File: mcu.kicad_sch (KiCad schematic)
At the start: 16 parts, among them J2 USB_C_Receptacle_USB2.0, J3 SH-6P, SW1 SW_Push, SW2 SW_Push, U3 TJA1051TK-3, U4 STM32G0B1KBU6

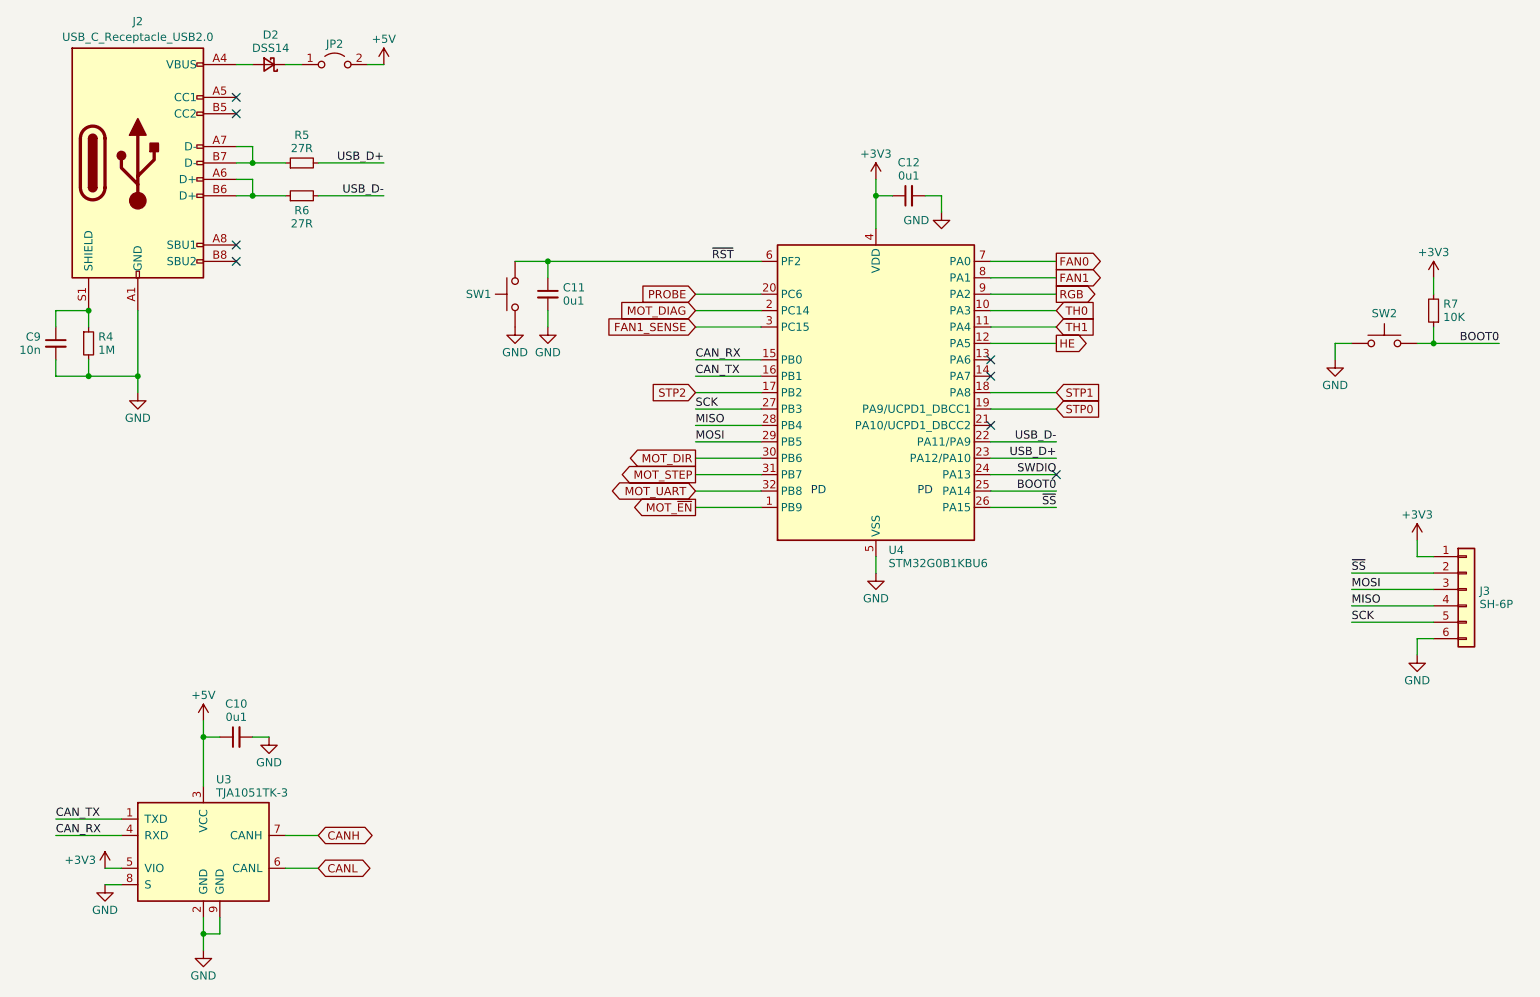
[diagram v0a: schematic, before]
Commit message: Added solder jumpers for CAN/USB interface selection
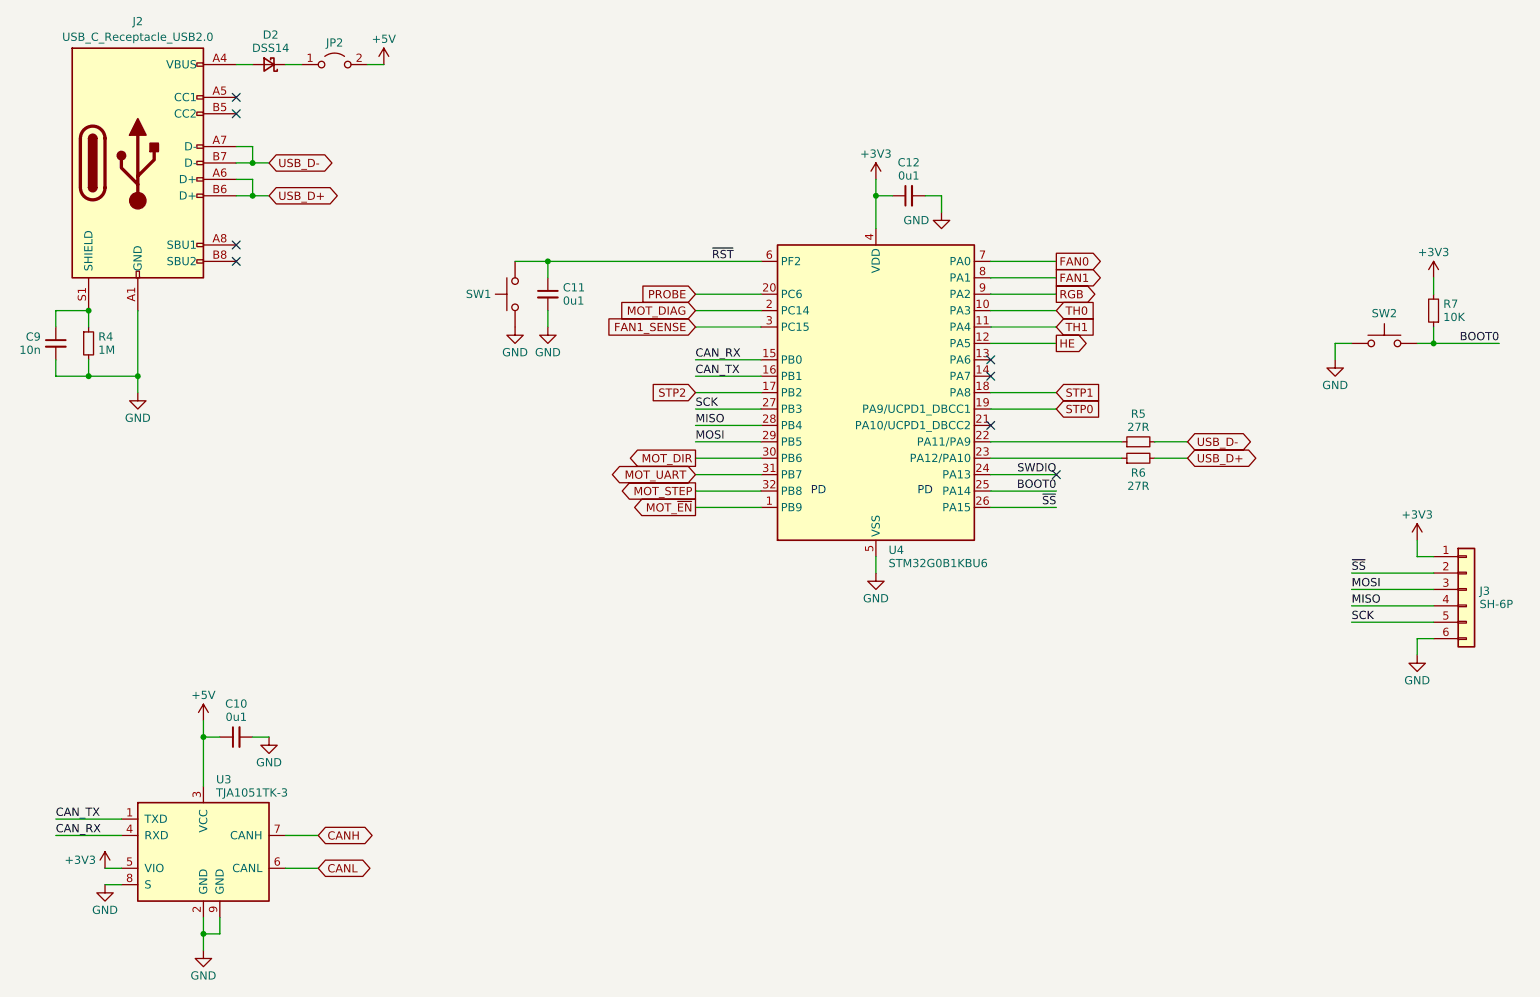
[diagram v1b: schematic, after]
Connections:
- net MOT_STEP: now also U4.32 (PB8); no longer U4.31 (PB7)
- net MOT_UART: now also U4.31 (PB7); no longer U4.32 (PB8)
- net USB_D+: now also J2.A6 (D+), J2.B6 (D+), R6.2; no longer R5.2, U4.23 (PA12/PA10)
- net USB_D-: now also J2.A7 (D-), J2.B7 (D-), R5.2; no longer R6.2, U4.22 (PA11/PA9)
- new net: R5.1, U4.22 (PA11/PA9)
- new net: R6.1, U4.23 (PA12/PA10)
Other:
- moved on the sheet: R5, R6
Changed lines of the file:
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@@
 	(paper "A4")
+	(junction
+		(at 50.8 137.16)
+		(diameter 0)
+		(color 0 0 0 0)
+	)
+	(junction
+		(at 241.3 76.2)
+		(diameter 0)
+		(color 0 0 0 0)
+	)
+	(junction
+		(at 40.64 81.28)
+		(diameter 0)
+		(color 0 0 0 0)
+	)
+	(junction
+		(at 50.8 167.64)
+		(diameter 0)
+		(color 0 0 0 0)
+	)
+	(junction
+		(at 154.94 53.34)
+		(diameter 0)
+		(color 0 0 0 0)
+	)
 	(junction
 		(at 58.42 53.34)
@@
 	)
 	(junction
-		(at 50.8 137.16)
+		(at 33.02 71.12)
 		(diameter 0)
 		(color 0 0 0 0)
 	)
 	(junction
-		(at 241.3 76.2)
-		(diameter 0)
-		(color 0 0 0 0)
-	)
-	(junction
-		(at 40.64 81.28)
-		(diameter 0)
-		(color 0 0 0 0)
-	)
-	(junction
-		(at 50.8 167.64)
-		(diameter 0)
-		(color 0 0 0 0)
-	)
-	(junction
-		(at 154.94 53.34)
-		(diameter 0)
-		(color 0 0 0 0)
-	)
-	(junction
-		(at 33.02 71.12)
+		(at 58.42 48.26)
 		(diameter 0)
 		(color 0 0 0 0)
@@
 		(color 0 0 0 0)
 	)
-	(junction
-		(at 58.42 48.26)
-		(diameter 0)
-		(color 0 0 0 0)
-	)
 	(no_connect
 		(at 172.72 88.9)
@@
 	(wire
 		(pts
+			(xy 58.42 48.26) (xy 60.96 48.26)
+		)
+		(stroke
+			(width 0)
+			(type default)
+		)
+	)
+	(wire
+		(pts
 			(xy 27.94 81.28) (xy 27.94 78.74)
 		)
@@
 	(wire
 		(pts
-			(xy 172.72 93.98) (xy 182.88 93.98)
+			(xy 172.72 93.98) (xy 193.04 93.98)
 		)
 		(stroke
@@
 	(wire
 		(pts
+			(xy 58.42 53.34) (xy 60.96 53.34)
+		)
+		(stroke
+			(width 0)
+			(type default)
+		)
+	)
+	(wire
+		(pts
 			(xy 137.16 86.36) (xy 127 86.36)
 		)
@@
 	(wire
 		(pts
-			(xy 172.72 91.44) (xy 182.88 91.44)
+			(xy 172.72 91.44) (xy 193.04 91.44)
 		)
 		(stroke
@@
 	(wire
 		(pts
-			(xy 68.58 53.34) (xy 78.74 53.34)
+			(xy 198.12 93.98) (xy 203.2 93.98)
 		)
 		(stroke
@@
 	(wire
 		(pts
-			(xy 58.42 48.26) (xy 63.5 48.26)
-		)
-		(stroke
-			(width 0)
-			(type default)
-		)
-	)
-	(wire
-		(pts
 			(xy 53.34 165.1) (xy 53.34 167.64)
 		)
@@
 	(wire
 		(pts
-			(xy 68.58 48.26) (xy 78.74 48.26)
+			(xy 198.12 91.44) (xy 203.2 91.44)
 		)
 		(stroke
@@
 		(pts
 			(xy 172.72 73.66) (xy 182.88 73.66)
-		)
-		(stroke
-			(width 0)
-			(type default)
-		)
-	)
-	(wire
-		(pts
-			(xy 58.42 53.34) (xy 63.5 53.34)
 		)
 		(stroke
@@
 		)
 	)
-	(label "USB_D+"
-		(at 182.88 93.98 180)
-		(fields_autoplaced yes)
-		(effects
-			(font
-				(size 1.27 1.27)
-			)
-			(justify right bottom)
-		)
-	)
 	(label "CAN_RX"
 		(at 127 78.74 0)
@@
 		)
 	)
-	(label "USB_D-"
-		(at 78.74 53.34 180)
-		(fields_autoplaced yes)
-		(effects
-			(font
-				(size 1.27 1.27)
-			)
-			(justify right bottom)
-		)
-	)
 	(label "CAN_TX"
 		(at 27.94 149.86 0)
@@
 		)
 	)
-	(label "USB_D-"
-		(at 182.88 91.44 180)
-		(fields_autoplaced yes)
-		(effects
-			(font
-				(size 1.27 1.27)
-			)
-			(justify right bottom)
-		)
-	)
 	(label "CAN_TX"
 		(at 127 81.28 0)
@@
 		)
 	)
-	(label "USB_D+"
-		(at 78.74 48.26 180)
-		(fields_autoplaced yes)
-		(effects
-			(font
-				(size 1.27 1.27)
-			)
-			(justify right bottom)
-		)
-	)
 	(label "BOOT0"
 		(at 182.88 99.06 180)
@@
 			)
 			(justify left bottom)
+		)
+	)
+	(global_label "USB_D+"
+		(shape bidirectional)
+		(at 203.2 93.98 0)
+		(fields_autoplaced yes)
+		(effects
+			(font
+				(size 1.27 1.27)
+			)
+			(justify left)
+		)
+		(property "Intersheetrefs" "${INTERSHEET_REFS}"
+			(at 214.9165 93.98 0)
+			(effects
+				(font
+					(size 1.27 1.27)
+				)
+				(justify left)
+				(hide yes)
+			)
 		)
 	)
@@
 		)
 	)
+	(global_label "USB_D-"
+		(shape bidirectional)
+		(at 60.96 48.26 0)
+		(fields_autoplaced yes)
+		(effects
+			(font
+				(size 1.27 1.27)
+			)
+			(justify left)
+		)
+		(property "Intersheetrefs" "${INTERSHEET_REFS}"
+			(at 72.6765 48.26 0)
+			(effects
+				(font
+					(size 1.27 1.27)
+				)
+				(justify left)
+				(hide yes)
+			)
+		)
+	)
 	(global_label "MOT_UART"
 		(shape bidirectional)
-		(at 127 99.06 180)
+		(at 127 96.52 180)
 		(fields_autoplaced yes)
 		(effects
@@
 		)
 		(property "Intersheetrefs" "${INTERSHEET_REFS}"
-			(at 113.6091 99.06 0)
+			(at 113.6091 96.52 0)
 			(effects
 				(font
@@
 	(global_label "MOT_STEP"
 		(shape output)
-		(at 127 96.52 180)
+		(at 127 99.06 180)
 		(fields_autoplaced yes)
 		(effects
@@
 		)
 		(property "Intersheetrefs" "${INTERSHEET_REFS}"
-			(at 114.781 96.52 0)
+			(at 114.781 99.06 0)
 			(effects
 				(font
@@
 				)
 				(justify right)
+				(hide yes)
+			)
+		)
+	)
+	(global_label "USB_D-"
+		(shape bidirectional)
+		(at 203.2 91.44 0)
+		(fields_autoplaced yes)
+		(effects
+			(font
+				(size 1.27 1.27)
+			)
+			(justify left)
+		)
+		(property "Intersheetrefs" "${INTERSHEET_REFS}"
+			(at 214.9165 91.44 0)
+			(effects
+				(font
+					(size 1.27 1.27)
+				)
+				(justify left)
+				(hide yes)
+			)
+		)
+	)
+	(global_label "USB_D+"
+		(shape bidirectional)
+		(at 60.96 53.34 0)
+		(fields_autoplaced yes)
+		(effects
+			(font
+				(size 1.27 1.27)
+			)
+			(justify left)
+		)
+		(property "Intersheetrefs" "${INTERSHEET_REFS}"
+			(at 72.6765 53.34 0)
+			(effects
+				(font
+					(size 1.27 1.27)
+				)
+				(justify left)
 				(hide yes)
 			)
@@
 		(fields_autoplaced yes)
 		(property "Reference" "JP2"
-			(at 71.12 29.837 0)
+			(at 71.12 29.6489 0)
 			(effects
 				(font
@@
 			)
 		)
-		(property "Description" ""
+		(property "Description" "Jumper, 2-pole, open"
 			(at 71.12 33.02 0)
 			(effects
@@
 	(symbol
 		(lib_id "Device:R_Small")
-		(at 66.04 48.26 90)
+		(at 195.58 91.44 90)
 		(unit 1)
 		(exclude_from_sim no)
@@
 		(fields_autoplaced yes)
 		(property "Reference" "R5"
-			(at 66.04 43.9434 90)
+			(at 195.58 87.1234 90)
 			(effects
 				(font
@@
 		)
 		(property "Value" "27R"
-			(at 66.04 45.9914 90)
+			(at 195.58 89.1714 90)
 			(effects
 				(font
@@
 		)
 		(property "Footprint" "Resistor_SMD:R_0402_1005Metric"
-			(at 66.04 48.26 0)
+			(at 195.58 91.44 0)
 			(effects
 				(font
@@
 		)
 		(property "Datasheet" "~"
-			(at 66.04 48.26 0)
+			(at 195.58 91.44 0)
 			(effects
 				(font
@@
 		)
 		(property "Description" ""
-			(at 66.04 48.26 0)
+			(at 195.58 91.44 0)
 			(effects
 				(font
@@
 		)
 		(property "MPN" ""
-			(at 66.04 48.26 0)
+			(at 195.58 91.44 0)
 			(effects
 				(font
@@
 		)
 		(property "LCSC" "C25100"
-			(at 66.04 48.26 0)
+			(at 195.58 91.44 0)
 			(effects
 				(font
@@
 	(symbol
 		(lib_id "Device:R_Small")
-		(at 66.04 53.34 90)
+		(at 195.58 93.98 90)
 		(unit 1)
 		(exclude_from_sim no)
@@
 		(fields_autoplaced yes)
 		(property "Reference" "R6"
-			(at 66.04 55.6086 90)
+			(at 195.58 96.2486 90)
 			(effects
 				(font
@@
 		)
 		(property "Value" "27R"
-			(at 66.04 57.6566 90)
+			(at 195.58 98.2966 90)
 			(effects
 				(font
@@
 		)
 		(property "Footprint" "Resistor_SMD:R_0402_1005Metric"
-			(at 66.04 53.34 0)
+			(at 195.58 93.98 0)
 			(effects
 				(font
@@
 		)
 		(property "Datasheet" "~"
-			(at 66.04 53.34 0)
+			(at 195.58 93.98 0)
 			(effects
 				(font
@@
 		)
 		(property "Description" ""
-			(at 66.04 53.34 0)
+			(at 195.58 93.98 0)
 			(effects
 				(font
@@
 		)
 		(property "MPN" ""
-			(at 66.04 53.34 0)
+			(at 195.58 93.98 0)
 			(effects
 				(font
@@
 		)
 		(property "LCSC" "C25100"
-			(at 66.04 53.34 0)
-			(effects
-				(font
+			(at 195.58 93.98 0)
+			(effects
+				(font

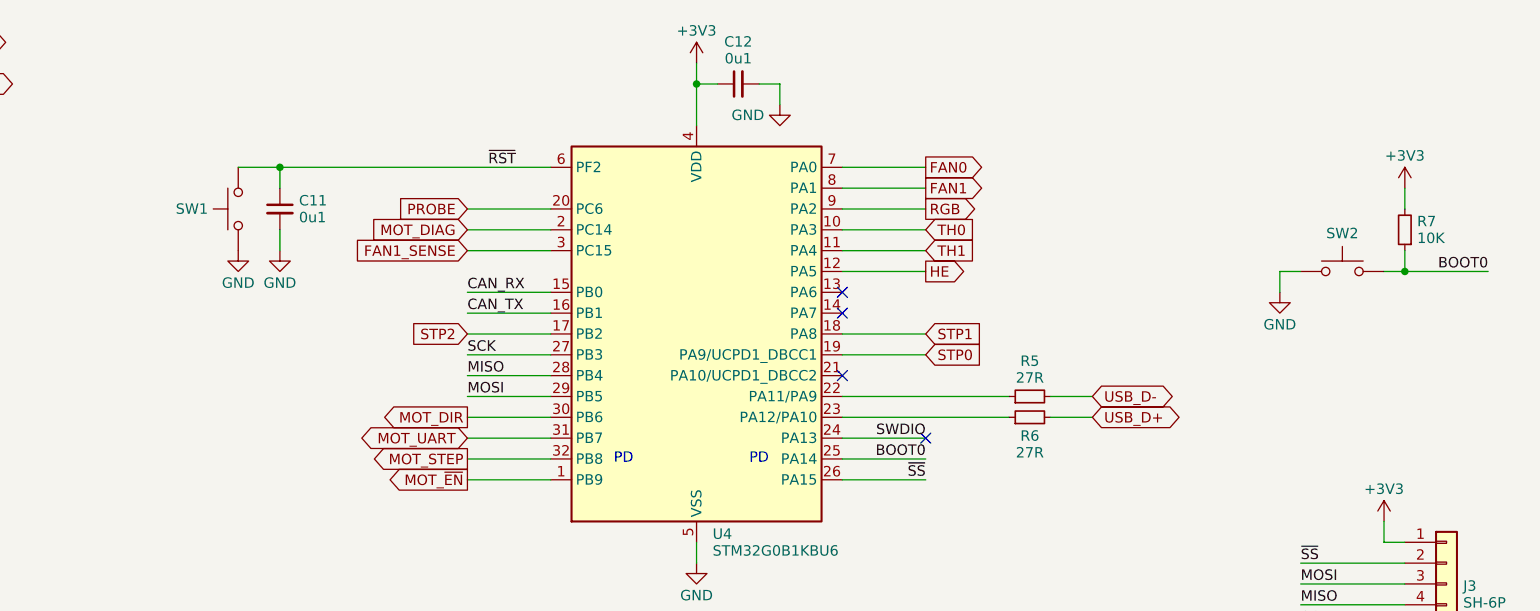
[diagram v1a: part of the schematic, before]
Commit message: Layout tweaks/pinout optimization
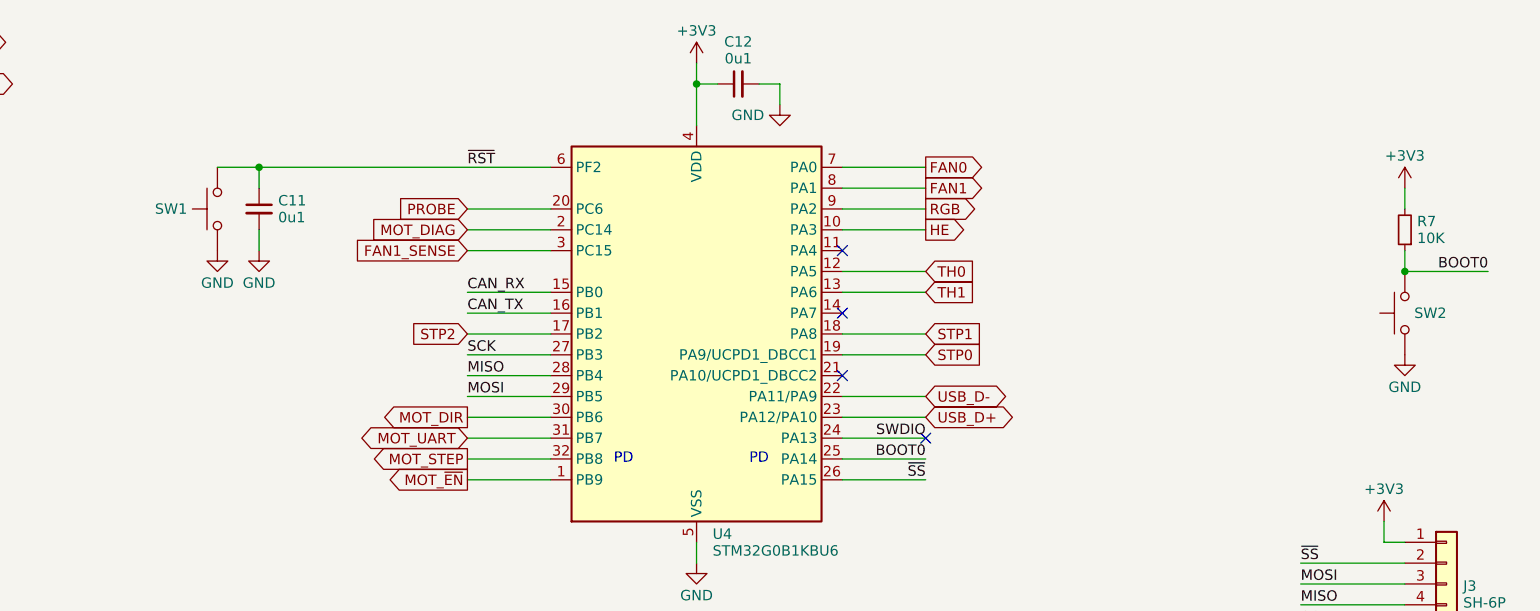
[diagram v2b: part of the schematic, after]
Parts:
- removed R5, R6: 27R, Resistor_SMD:R_0402_1005Metric, symbol Device:R_Small
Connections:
- net HE: now also U4.10 (PA3); no longer U4.12 (PA5)
- net TH0: now also U4.12 (PA5); no longer U4.10 (PA3)
- net TH1: now also U4.13 (PA6); no longer U4.11 (PA4)
- net USB_D+: now also U4.23 (PA12/PA10)
- net USB_D-: now also U4.22 (PA11/PA9)
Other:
- moved on the sheet: C11, SW1, SW2
